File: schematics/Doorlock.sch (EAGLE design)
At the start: 40 parts, among them IC1 AT90S2313S, J1 RJ45, K1 G5V1, K2 G5V1, X1 RASPI_BOARD_B+#_H, X2 RIA182-04, X4 RIA182-05

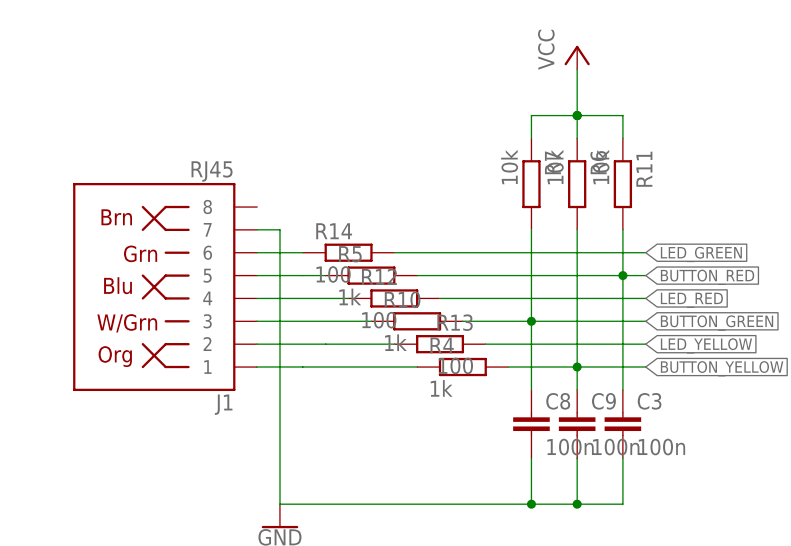
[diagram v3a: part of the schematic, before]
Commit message: schematics: Update Resistor values
Signed-off-by: Ralf Ramsauer <ralf@binary-kitchen.de>
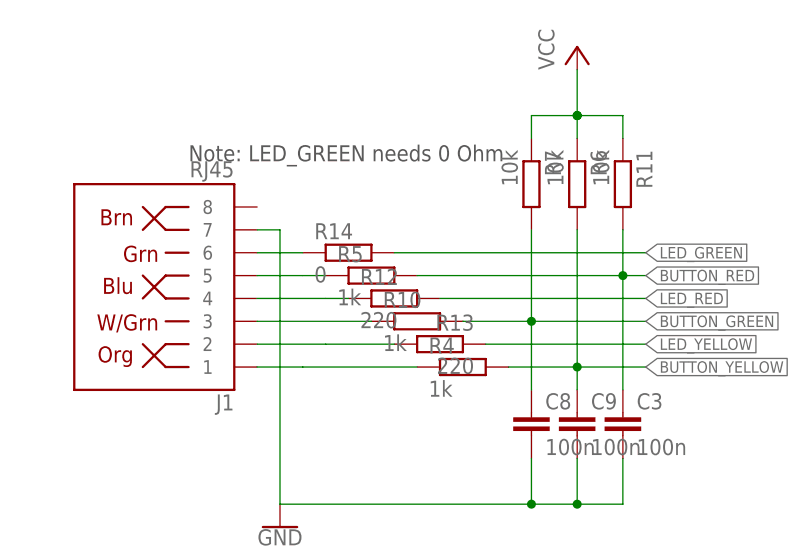
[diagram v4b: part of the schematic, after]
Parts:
- R12, R13: value 100 -> 220
- R14: value 100 -> 0
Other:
- note added: "Note: LED_GREEN needs 0 Ohm"
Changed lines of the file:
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@@
 <grid distance="0.1" unitdist="inch" unit="inch" style="lines" multiple="1" display="no" altdistance="0.01" altunitdist="inch" altunit="inch"/>
 <layers>
-<layer number="1" name="Top" color="4" fill="1" visible="yes" active="no"/>
-<layer number="2" name="Route2" color="16" fill="1" visible="yes" active="no"/>
-<layer number="3" name="Route3" color="17" fill="1" visible="yes" active="no"/>
-<layer number="4" name="Route4" color="18" fill="1" visible="yes" active="no"/>
-<layer number="5" name="Route5" color="19" fill="1" visible="yes" active="no"/>
-<layer number="6" name="Route6" color="25" fill="1" visible="yes" active="no"/>
-<layer number="7" name="Route7" color="26" fill="1" visible="yes" active="no"/>
-<layer number="8" name="Route8" color="27" fill="1" visible="yes" active="no"/>
-<layer number="9" name="Route9" color="28" fill="1" visible="yes" active="no"/>
-<layer number="10" name="Route10" color="29" fill="1" visible="yes" active="no"/>
-<layer number="11" name="Route11" color="30" fill="1" visible="yes" active="no"/>
-<layer number="12" name="Route12" color="20" fill="1" visible="yes" active="no"/>
-<layer number="13" name="Route13" color="21" fill="1" visible="yes" active="no"/>
-<layer number="14" name="Route14" color="22" fill="1" visible="yes" active="no"/>
-<layer number="15" name="Route15" color="23" fill="1" visible="yes" active="no"/>
-<layer number="16" name="Bottom" color="1" fill="1" visible="yes" active="no"/>
-<layer number="17" name="Pads" color="2" fill="1" visible="yes" active="no"/>
-<layer number="18" name="Vias" color="2" fill="1" visible="yes" active="no"/>
-<layer number="19" name="Unrouted" color="6" fill="1" visible="yes" active="no"/>
-<layer number="20" name="Dimension" color="24" fill="1" visible="yes" active="no"/>
-<layer number="21" name="tPlace" color="7" fill="1" visible="yes" active="no"/>
-<layer number="22" name="bPlace" color="7" fill="1" visible="yes" active="no"/>
-<layer number="23" name="tOrigins" color="15" fill="1" visible="yes" active="no"/>
-<layer number="24" name="bOrigins" color="15" fill="1" visible="yes" active="no"/>
-<layer number="25" name="tNames" color="7" fill="1" visible="yes" active="no"/>
-<layer number="26" name="bNames" color="7" fill="1" visible="yes" active="no"/>
-<layer number="27" name="tValues" color="7" fill="1" visible="yes" active="no"/>
-<layer number="28" name="bValues" color="7" fill="1" visible="yes" active="no"/>
+<layer number="1" name="Top" color="4" fill="1" visible="no" active="no"/>
+<layer number="2" name="Route2" color="16" fill="1" visible="no" active="no"/>
+<layer number="3" name="Route3" color="17" fill="1" visible="no" active="no"/>
+<layer number="4" name="Route4" color="18" fill="1" visible="no" active="no"/>
+<layer number="5" name="Route5" color="19" fill="1" visible="no" active="no"/>
+<layer number="6" name="Route6" color="25" fill="1" visible="no" active="no"/>
+<layer number="7" name="Route7" color="26" fill="1" visible="no" active="no"/>
+<layer number="8" name="Route8" color="27" fill="1" visible="no" active="no"/>
+<layer number="9" name="Route9" color="28" fill="1" visible="no" active="no"/>
+<layer number="10" name="Route10" color="29" fill="1" visible="no" active="no"/>
+<layer number="11" name="Route11" color="30" fill="1" visible="no" active="no"/>
+<layer number="12" name="Route12" color="20" fill="1" visible="no" active="no"/>
+<layer number="13" name="Route13" color="21" fill="1" visible="no" active="no"/>
+<layer number="14" name="Route14" color="22" fill="1" visible="no" active="no"/>
+<layer number="15" name="Route15" color="23" fill="1" visible="no" active="no"/>
+<layer number="16" name="Bottom" color="1" fill="1" visible="no" active="no"/>
+<layer number="17" name="Pads" color="2" fill="1" visible="no" active="no"/>
+<layer number="18" name="Vias" color="2" fill="1" visible="no" active="no"/>
+<layer number="19" name="Unrouted" color="6" fill="1" visible="no" active="no"/>
+<layer number="20" name="Dimension" color="24" fill="1" visible="no" active="no"/>
+<layer number="21" name="tPlace" color="7" fill="1" visible="no" active="no"/>
+<layer number="22" name="bPlace" color="7" fill="1" visible="no" active="no"/>
+<layer number="23" name="tOrigins" color="15" fill="1" visible="no" active="no"/>
+<layer number="24" name="bOrigins" color="15" fill="1" visible="no" active="no"/>
+<layer number="25" name="tNames" color="7" fill="1" visible="no" active="no"/>
+<layer number="26" name="bNames" color="7" fill="1" visible="no" active="no"/>
+<layer number="27" name="tValues" color="7" fill="1" visible="no" active="no"/>
+<layer number="28" name="bValues" color="7" fill="1" visible="no" active="no"/>
 <layer number="29" name="tStop" color="7" fill="3" visible="no" active="no"/>
 <layer number="30" name="bStop" color="7" fill="6" visible="no" active="no"/>
@@
 <layer number="35" name="tGlue" color="7" fill="4" visible="no" active="no"/>
 <layer number="36" name="bGlue" color="7" fill="5" visible="no" active="no"/>
-<layer number="37" name="tTest" color="7" fill="1" visible="yes" active="no"/>
-<layer number="38" name="bTest" color="7" fill="1" visible="yes" active="no"/>
+<layer number="37" name="tTest" color="7" fill="1" visible="no" active="no"/>
+<layer number="38" name="bTest" color="7" fill="1" visible="no" active="no"/>
 <layer number="39" name="tKeepout" color="4" fill="11" visible="no" active="no"/>
 <layer number="40" name="bKeepout" color="1" fill="11" visible="no" active="no"/>
@@
 <layer number="44" name="Drills" color="7" fill="1" visible="no" active="no"/>
 <layer number="45" name="Holes" color="7" fill="1" visible="no" active="no"/>
-<layer number="46" name="Milling" color="3" fill="1" visible="yes" active="no"/>
-<layer number="47" name="Measures" color="7" fill="1" visible="yes" active="no"/>
-<layer number="48" name="Document" color="7" fill="1" visible="yes" active="no"/>
-<layer number="49" name="Reference" color="7" fill="1" visible="yes" active="no"/>
-<layer number="50" name="dxf" color="7" fill="1" visible="yes" active="no"/>
-<layer number="51" name="tDocu" color="7" fill="1" visible="yes" active="no"/>
-<layer number="52" name="bDocu" color="7" fill="1" visible="yes" active="no"/>
-<layer number="53" name="tGND_GNDA" color="7" fill="9" visible="yes" active="no"/>
-<layer number="54" name="bGND_GNDA" color="1" fill="9" visible="yes" active="no"/>
-<layer number="56" name="wert" color="7" fill="1" visible="yes" active="no"/>
-<layer number="57" name="tCAD" color="7" fill="1" visible="yes" active="no"/>
-<layer number="59" name="tCarbon" color="7" fill="1" visible="yes" active="no"/>
-<layer number="60" name="bCarbon" color="7" fill="1" visible="yes" active="no"/>
+<layer number="46" name="Milling" color="3" fill="1" visible="no" active="no"/>
+<layer number="47" name="Measures" color="7" fill="1" visible="no" active="no"/>
+<layer number="48" name="Document" color="7" fill="1" visible="no" active="no"/>
+<layer number="49" name="Reference" color="7" fill="1" visible="no" active="no"/>
+<layer number="50" name="dxf" color="7" fill="1" visible="no" active="no"/>
+<layer number="51" name="tDocu" color="7" fill="1" visible="no" active="no"/>
+<layer number="52" name="bDocu" color="7" fill="1" visible="no" active="no"/>
+<layer number="53" name="tGND_GNDA" color="7" fill="9" visible="no" active="no"/>
+<layer number="54" name="bGND_GNDA" color="1" fill="9" visible="no" active="no"/>
+<layer number="56" name="wert" color="7" fill="1" visible="no" active="no"/>
+<layer number="57" name="tCAD" color="7" fill="1" visible="no" active="no"/>
+<layer number="59" name="tCarbon" color="7" fill="1" visible="no" active="no"/>
+<layer number="60" name="bCarbon" color="7" fill="1" visible="no" active="no"/>
 <layer number="88" name="SimResults" color="9" fill="1" visible="yes" active="yes"/>
 <layer number="89" name="SimProbes" color="9" fill="1" visible="yes" active="yes"/>
@@
 <part name="R11" library="rcl" deviceset="R-EU_" device="R0805" value="10k"/>
 <part name="C3" library="rcl" deviceset="C-EU" device="C0805" value="100n"/>
-<part name="R12" library="rcl" deviceset="R-EU_" device="R0805" value="100"/>
-<part name="R13" library="rcl" deviceset="R-EU_" device="R0805" value="100"/>
-<part name="R14" library="rcl" deviceset="R-EU_" device="R0805" value="100"/>
+<part name="R12" library="rcl" deviceset="R-EU_" device="R0805" value="220"/>
+<part name="R13" library="rcl" deviceset="R-EU_" device="R0805" value="220"/>
+<part name="R14" library="rcl" deviceset="R-EU_" device="R0805" value="0"/>
 <part name="D1" library="diode" library_urn="urn:adsk.eagle:library:210" deviceset="CGRM400*-G" device="" package3d_urn="urn:adsk.eagle:package:43457/2" technology="2"/>
 <part name="D2" library="diode" library_urn="urn:adsk.eagle:library:210" deviceset="CGRM400*-G" device="" package3d_urn="urn:adsk.eagle:package:43457/2" technology="2"/>
@@
 <sheet>
 <plain>
+<text x="22.86" y="198.12" size="1.778" layer="97">Note: LED_GREEN needs 0 Ohm</text>
 </plain>
 <instances>

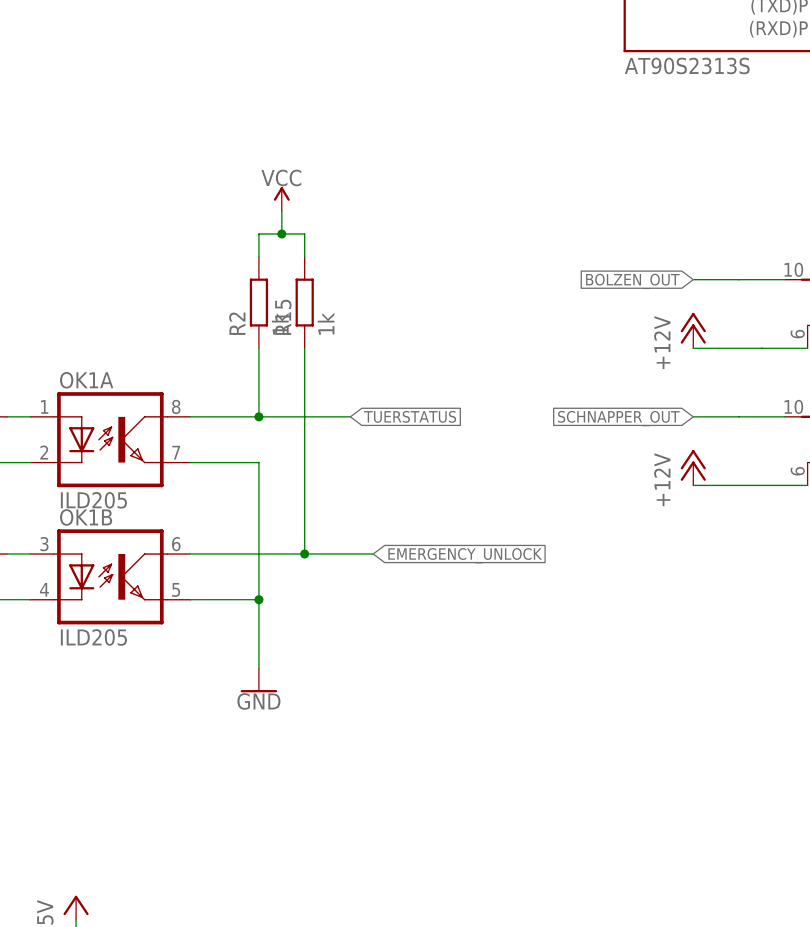
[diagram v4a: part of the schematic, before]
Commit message: schematics: decouple optocoupler
Signed-off-by: Ralf Ramsauer <ralf@binary-kitchen.de>
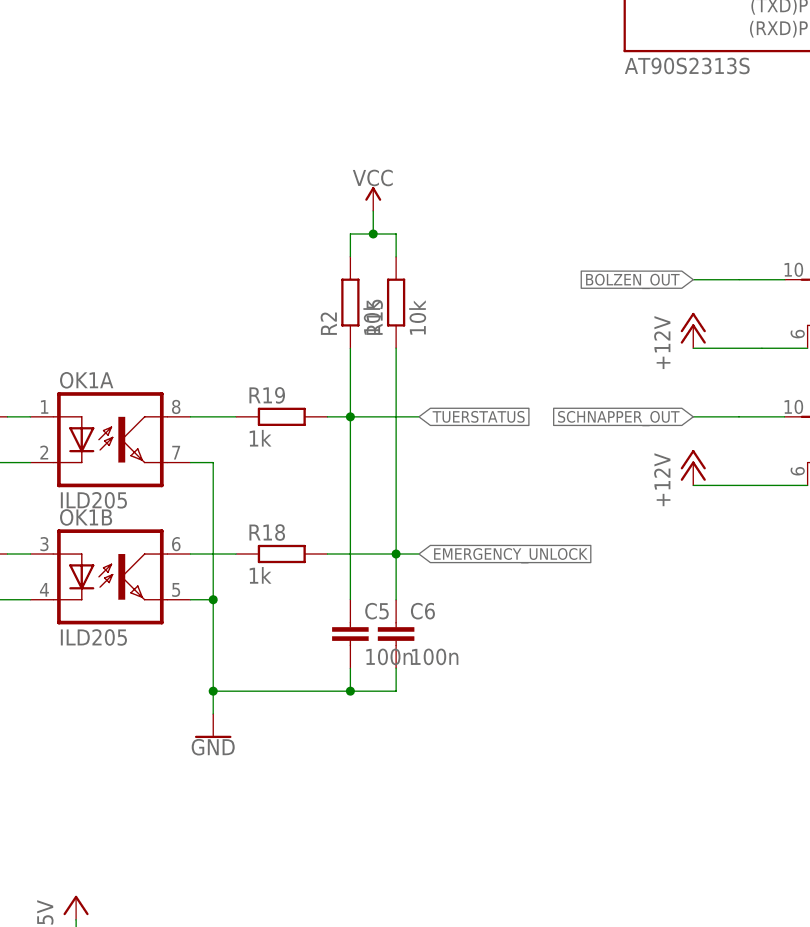
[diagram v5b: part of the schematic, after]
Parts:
- added C5, C6: 100n, rcl:C-EUC0805
- added R18, R19: 1k, rcl:R-EU_R0805
- R15, R2: value 1k -> 10k
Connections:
- new net N$3: OK1B.COL, R18.1
- new net N$5: OK1A.COL, R19.1
- net EMERGENCY_UNLOCK: now also C6.1, R18.2; no longer OK1B.COL
- net GND: now also C5.2, C6.2
- net TUERSTATUS: now also C5.1, R19.2; no longer OK1A.COL
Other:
- moved on the sheet: R15, R2
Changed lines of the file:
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@@
 <part name="SUPPLY2" library="supply2" library_urn="urn:adsk.eagle:library:372" deviceset="GND2" device=""/>
 <part name="R1" library="rcl" deviceset="R-EU_" device="R0805" value="1k"/>
-<part name="R2" library="rcl" deviceset="R-EU_" device="R0805" value="1k"/>
+<part name="R2" library="rcl" deviceset="R-EU_" device="R0805" value="10k"/>
 <part name="SUPPLY3" library="SparkFun-PowerSymbols" library_urn="urn:adsk.eagle:library:530" deviceset="VCC" device=""/>
 <part name="GND3" library="SparkFun-PowerSymbols" library_urn="urn:adsk.eagle:library:530" deviceset="GND" device=""/>
 <part name="R3" library="rcl" deviceset="R-EU_" device="R0805" value="1k"/>
-<part name="R15" library="rcl" deviceset="R-EU_" device="R0805" value="1k"/>
+<part name="R15" library="rcl" deviceset="R-EU_" device="R0805" value="10k"/>
 <part name="P+5" library="supply1" library_urn="urn:adsk.eagle:library:371" deviceset="+5V" device=""/>
 <part name="P+8" library="supply1" deviceset="+12V" device=""/>
@@
 <part name="JP1" library="pinhead" library_urn="urn:adsk.eagle:library:325" deviceset="PINHD-1X2" device="" package3d_urn="urn:adsk.eagle:package:22435/2"/>
 <part name="J1" library="SparkFun-Connectors" library_urn="urn:adsk.eagle:library:513" deviceset="RJ45-8" device="" package3d_urn="urn:adsk.eagle:package:38235/1" value="RJ45"/>
+<part name="C5" library="rcl" deviceset="C-EU" device="C0805" value="100n"/>
+<part name="C6" library="rcl" deviceset="C-EU" device="C0805" value="100n"/>
+<part name="R18" library="rcl" deviceset="R-EU_" device="R0805" value="1k"/>
+<part name="R19" library="rcl" deviceset="R-EU_" device="R0805" value="1k"/>
 </parts>
 <sheets>
@@
 <instance part="SUPPLY2" gate="G$1" x="45.72" y="55.88" rot="MR0"/>
 <instance part="R1" gate="G$1" x="53.34" y="83.82"/>
-<instance part="R2" gate="G$1" x="86.36" y="96.52" rot="R90"/>
-<instance part="SUPPLY3" gate="G$1" x="88.9" y="106.68"/>
-<instance part="GND3" gate="1" x="86.36" y="53.34"/>
+<instance part="R2" gate="G$1" x="96.52" y="96.52" rot="R90"/>
+<instance part="SUPPLY3" gate="G$1" x="99.06" y="106.68"/>
+<instance part="GND3" gate="1" x="81.28" y="48.26"/>
 <instance part="R3" gate="G$1" x="53.34" y="68.58"/>
-<instance part="R15" gate="G$1" x="91.44" y="96.52" rot="R90"/>
+<instance part="R15" gate="G$1" x="101.6" y="96.52" rot="R90"/>
 <instance part="P+5" gate="1" x="182.88" y="96.52"/>
 <instance part="P+8" gate="1" x="134.62" y="78.74"/>
@@
 <instance part="JP1" gate="G$1" x="116.84" y="175.26" rot="R180"/>
 <instance part="J1" gate="JP1" x="22.86" y="182.88" rot="R180"/>
+<instance part="C5" gate="G$1" x="96.52" y="60.96"/>
+<instance part="C6" gate="G$1" x="101.6" y="60.96"/>
+<instance part="R18" gate="G$1" x="88.9" y="68.58"/>
+<instance part="R19" gate="G$1" x="88.9" y="83.82"/>
 </instances>
 <busses>
@@
 <pinref part="SUPPLY3" gate="G$1" pin="VCC"/>
 <pinref part="R15" gate="G$1" pin="2"/>
-<wire x1="88.9" y1="104.14" x2="86.36" y2="104.14" width="0.1524" layer="91"/>
-<wire x1="88.9" y1="104.14" x2="88.9" y2="106.68" width="0.1524" layer="91"/>
-<junction x="88.9" y="104.14"/>
-<wire x1="86.36" y1="101.6" x2="86.36" y2="104.14" width="0.1524" layer="91"/>
-<wire x1="91.44" y1="101.6" x2="91.44" y2="104.14" width="0.1524" layer="91"/>
-<wire x1="88.9" y1="104.14" x2="91.44" y2="104.14" width="0.1524" layer="91"/>
+<wire x1="99.06" y1="104.14" x2="96.52" y2="104.14" width="0.1524" layer="91"/>
+<wire x1="99.06" y1="104.14" x2="99.06" y2="106.68" width="0.1524" layer="91"/>
+<junction x="99.06" y="104.14"/>
+<wire x1="96.52" y1="101.6" x2="96.52" y2="104.14" width="0.1524" layer="91"/>
+<wire x1="101.6" y1="101.6" x2="101.6" y2="104.14" width="0.1524" layer="91"/>
+<wire x1="99.06" y1="104.14" x2="101.6" y2="104.14" width="0.1524" layer="91"/>
 </segment>
 <segment>
@@
 <segment>
 <pinref part="OK1" gate="B" pin="EMIT"/>
-<wire x1="78.74" y1="63.5" x2="86.36" y2="63.5" width="0.1524" layer="91"/>
+<wire x1="78.74" y1="63.5" x2="81.28" y2="63.5" width="0.1524" layer="91"/>
 <pinref part="GND3" gate="1" pin="GND"/>
-<wire x1="86.36" y1="63.5" x2="86.36" y2="55.88" width="0.1524" layer="91"/>
+<wire x1="81.28" y1="63.5" x2="81.28" y2="53.34" width="0.1524" layer="91"/>
 <pinref part="OK1" gate="A" pin="EMIT"/>
-<wire x1="78.74" y1="78.74" x2="86.36" y2="78.74" width="0.1524" layer="91"/>
-<wire x1="86.36" y1="78.74" x2="86.36" y2="63.5" width="0.1524" layer="91"/>
-<junction x="86.36" y="63.5"/>
+<wire x1="81.28" y1="53.34" x2="81.28" y2="50.8" width="0.1524" layer="91"/>
+<wire x1="78.74" y1="78.74" x2="81.28" y2="78.74" width="0.1524" layer="91"/>
+<wire x1="81.28" y1="78.74" x2="81.28" y2="63.5" width="0.1524" layer="91"/>
+<junction x="81.28" y="63.5"/>
+<pinref part="C6" gate="G$1" pin="2"/>
+<wire x1="101.6" y1="55.88" x2="101.6" y2="53.34" width="0.1524" layer="91"/>
+<wire x1="101.6" y1="53.34" x2="96.52" y2="53.34" width="0.1524" layer="91"/>
+<junction x="81.28" y="53.34"/>
+<pinref part="C5" gate="G$1" pin="2"/>
+<wire x1="96.52" y1="53.34" x2="81.28" y2="53.34" width="0.1524" layer="91"/>
+<wire x1="96.52" y1="55.88" x2="96.52" y2="53.34" width="0.1524" layer="91"/>
+<junction x="96.52" y="53.34"/>
 </segment>
 <segment>
@@
 <segment>
 <pinref part="R15" gate="G$1" pin="1"/>
-<wire x1="91.44" y1="68.58" x2="91.44" y2="91.44" width="0.1524" layer="91"/>
-<wire x1="91.44" y1="68.58" x2="99.06" y2="68.58" width="0.1524" layer="91"/>
-<label x="99.06" y="68.58" size="1.27" layer="95" font="fixed" xref="yes"/>
-<pinref part="OK1" gate="B" pin="COL"/>
-<wire x1="78.74" y1="68.58" x2="91.44" y2="68.58" width="0.1524" layer="91"/>
-<junction x="91.44" y="68.58"/>
+<wire x1="101.6" y1="68.58" x2="101.6" y2="91.44" width="0.1524" layer="91"/>
+<wire x1="101.6" y1="68.58" x2="104.14" y2="68.58" width="0.1524" layer="91"/>
+<label x="104.14" y="68.58" size="1.27" layer="95" font="fixed" xref="yes"/>
+<pinref part="R18" gate="G$1" pin="2"/>
+<wire x1="93.98" y1="68.58" x2="101.6" y2="68.58" width="0.1524" layer="91"/>
+<junction x="101.6" y="68.58"/>
+<pinref part="C6" gate="G$1" pin="1"/>
+<wire x1="101.6" y1="68.58" x2="101.6" y2="63.5" width="0.1524" layer="91"/>
 </segment>
 </net>
@@
 <segment>
 <pinref part="R2" gate="G$1" pin="1"/>
-<wire x1="91.44" y1="83.82" x2="96.52" y2="83.82" width="0.1524" layer="91"/>
-<label x="96.52" y="83.82" size="1.27" layer="95" font="fixed" xref="yes"/>
-<pinref part="OK1" gate="A" pin="COL"/>
-<wire x1="78.74" y1="83.82" x2="86.36" y2="83.82" width="0.1524" layer="91"/>
-<wire x1="86.36" y1="83.82" x2="91.44" y2="83.82" width="0.1524" layer="91"/>
-<wire x1="86.36" y1="91.44" x2="86.36" y2="83.82" width="0.1524" layer="91"/>
-<junction x="86.36" y="83.82"/>
+<wire x1="93.98" y1="83.82" x2="96.52" y2="83.82" width="0.1524" layer="91"/>
+<label x="104.14" y="83.82" size="1.27" layer="95" font="fixed" xref="yes"/>
+<wire x1="96.52" y1="83.82" x2="104.14" y2="83.82" width="0.1524" layer="91"/>
+<pinref part="R19" gate="G$1" pin="2"/>
+<wire x1="96.52" y1="91.44" x2="96.52" y2="83.82" width="0.1524" layer="91"/>
+<junction x="96.52" y="83.82"/>
+<pinref part="C5" gate="G$1" pin="1"/>
+<wire x1="96.52" y1="83.82" x2="96.52" y2="63.5" width="0.1524" layer="91"/>
 </segment>
 <segment>
@@
 </segment>
 </net>
+<net name="N$3" class="0">
+<segment>
+<pinref part="OK1" gate="B" pin="COL"/>
+<pinref part="R18" gate="G$1" pin="1"/>
+<wire x1="78.74" y1="68.58" x2="83.82" y2="68.58" width="0.1524" layer="91"/>
+</segment>
+</net>
+<net name="N$5" class="0">
+<segment>
+<pinref part="OK1" gate="A" pin="COL"/>
+<pinref part="R19" gate="G$1" pin="1"/>
+<wire x1="78.74" y1="83.82" x2="83.82" y2="83.82" width="0.1524" layer="91"/>
+</segment>
+</net>
